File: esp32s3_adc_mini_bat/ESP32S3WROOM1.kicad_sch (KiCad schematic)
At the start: 5 parts, among them J4 Conn_01x22_Socket, J5 Conn_01x22_Socket, U2 ESP32-S3-WROOM-1

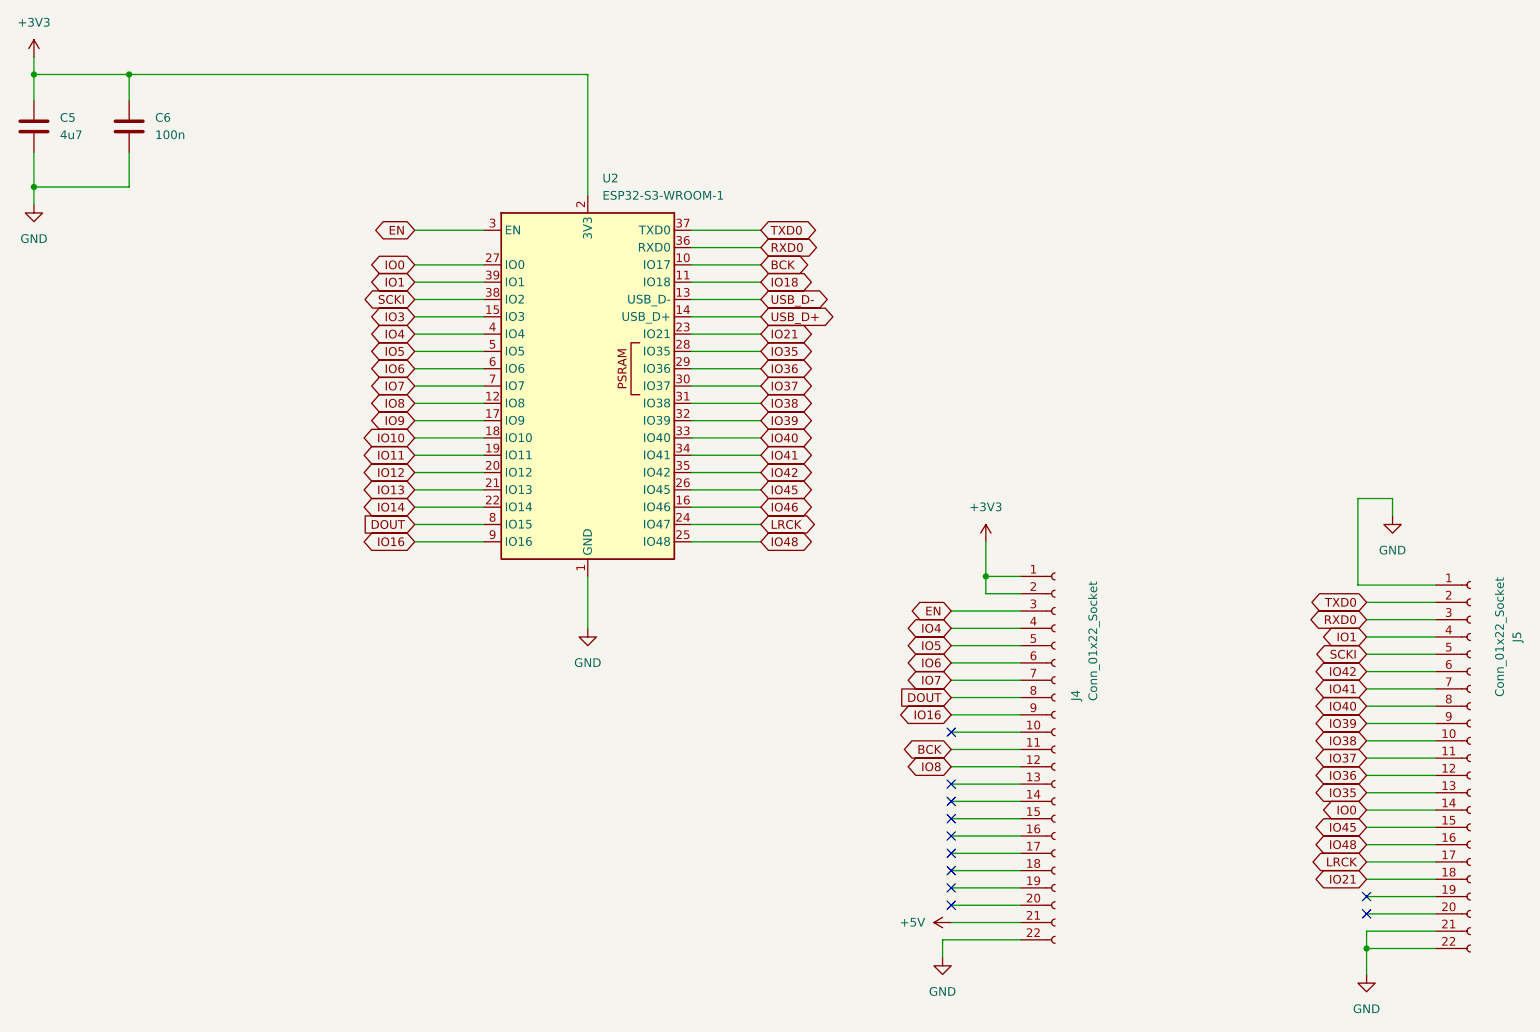
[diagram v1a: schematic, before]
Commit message: feat: schematic done and pcb grouping
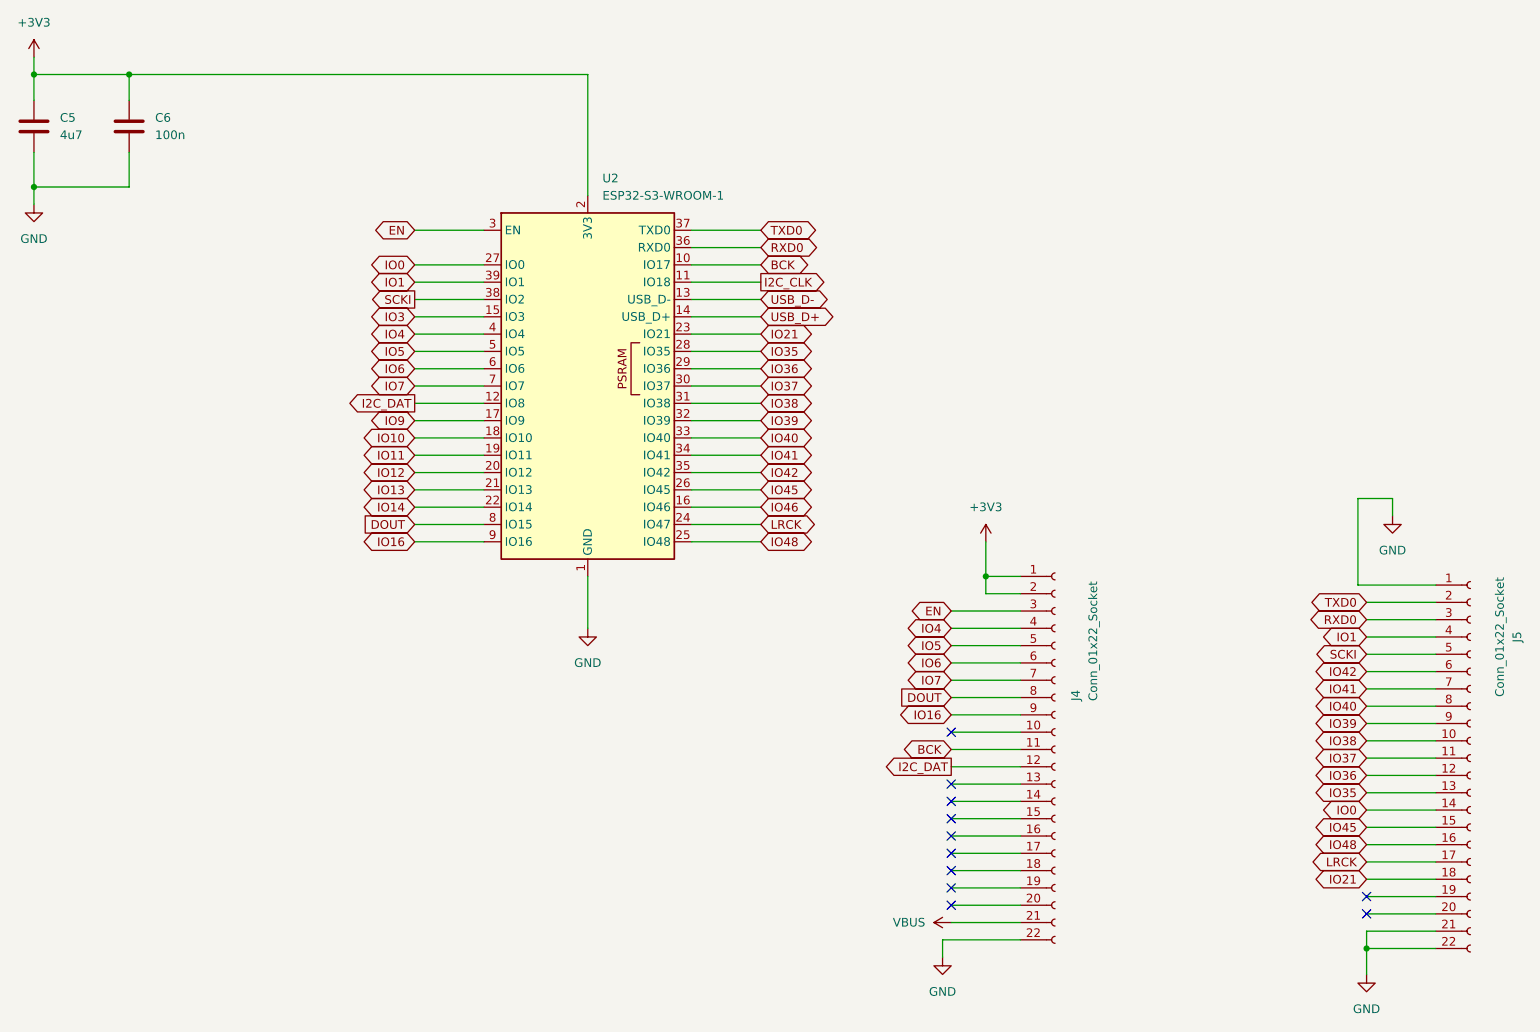
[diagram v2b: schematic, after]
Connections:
- net +5V renamed VBUS
- net IO18 renamed I2C_CLK
- net IO8 renamed I2C_DAT
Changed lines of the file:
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@@
+	(wire
+		(pts
+			(xy 160.02 144.78) (xy 170.18 144.78)
+		)
+		(stroke
+			(width 0)
+			(type default)
+		)
+	)
+	(wire
+		(pts
+			(xy 39.37 41.91) (xy 39.37 36.83)
+		)
+		(stroke
+			(width 0)
+			(type default)
+		)
+	)
+	(wire
+		(pts
+			(xy 25.4 25.4) (xy 25.4 29.21)
+		)
+		(stroke
+			(width 0)
+			(type default)
+		)
+	)
+	(wire
+		(pts
+			(xy 132.08 81.28) (xy 121.92 81.28)
+		)
+		(stroke
+			(width 0)
+			(type default)
+		)
+	)
+	(wire
+		(pts
+			(xy 220.98 133.35) (xy 231.14 133.35)
+		)
+		(stroke
+			(width 0)
+			(type default)
+		)
+	)
+	(wire
+		(pts
+			(xy 160.02 137.16) (xy 170.18 137.16)
+		)
+		(stroke
+			(width 0)
+			(type default)
+		)
+	)
 	(wire
 		(pts
@@
 	(wire
 		(pts
-			(xy 160.02 144.78) (xy 170.18 144.78)
-		)
-		(stroke
-			(width 0)
-			(type default)
-		)
-	)
-	(wire
-		(pts
-			(xy 39.37 41.91) (xy 39.37 36.83)
-		)
-		(stroke
-			(width 0)
-			(type default)
-		)
-	)
-	(wire
-		(pts
-			(xy 25.4 25.4) (xy 25.4 29.21)
-		)
-		(stroke
-			(width 0)
-			(type default)
-		)
-	)
-	(wire
-		(pts
-			(xy 132.08 81.28) (xy 121.92 81.28)
-		)
-		(stroke
-			(width 0)
-			(type default)
-		)
-	)
-	(wire
-		(pts
-			(xy 220.98 133.35) (xy 231.14 133.35)
-		)
-		(stroke
-			(width 0)
-			(type default)
-		)
-	)
-	(wire
-		(pts
-			(xy 160.02 137.16) (xy 170.18 137.16)
-		)
-		(stroke
-			(width 0)
-			(type default)
-		)
-	)
-	(wire
-		(pts
 			(xy 220.98 148.59) (xy 231.14 148.59)
 		)
@@
 	(wire
 		(pts
-			(xy 132.08 55.88) (xy 121.92 55.88)
+			(xy 121.92 55.88) (xy 132.08 55.88)
 		)
 		(stroke
@@
 		)
 	)
-	(global_label "IO8"
-		(shape bidirectional)
-		(at 160.02 127 180)
-		(fields_autoplaced yes)
-		(effects
-			(font
-				(size 1.27 1.27)
-			)
-			(justify right)
-		)
-		(property "Intersheetrefs" "${INTERSHEET_REFS}"
-			(at 152.7787 127 0)
-			(hide yes)
-			(show_name no)
-			(do_not_autoplace no)
-			(effects
-				(font
-					(size 1.27 1.27)
-				)
-				(justify right)
-			)
-		)
-	)
 	(global_label "IO36"
 		(shape bidirectional)
@@
 		)
 	)
-	(global_label "IO18"
-		(shape bidirectional)
+	(global_label "IO42"
+		(shape bidirectional)
+		(at 132.08 83.82 0)
+		(fields_autoplaced yes)
+		(effects
+			(font
+				(size 1.27 1.27)
+			)
+			(justify left)
+		)
+		(property "Intersheetrefs" "${INTERSHEET_REFS}"
+			(at 140.5308 83.82 0)
+			(hide yes)
+			(show_name no)
+			(do_not_autoplace no)
+			(effects
+				(font
+					(size 1.27 1.27)
+				)
+				(justify left)
+			)
+		)
+	)
+	(global_label "IO48"
+		(shape bidirectional)
+		(at 220.98 138.43 180)
+		(fields_autoplaced yes)
+		(effects
+			(font
+				(size 1.27 1.27)
+			)
+			(justify right)
+		)
+		(property "Intersheetrefs" "${INTERSHEET_REFS}"
+			(at 212.5292 138.43 0)
+			(hide yes)
+			(show_name no)
+			(do_not_autoplace no)
+			(effects
+				(font
+					(size 1.27 1.27)
+				)
+				(justify right)
+			)
+		)
+	)
+	(global_label "I2C_CLK"
+		(shape output)
 		(at 132.08 55.88 0)
 		(fields_autoplaced yes)
@@
 		)
 		(property "Intersheetrefs" "${INTERSHEET_REFS}"
-			(at 140.5308 55.88 0)
+			(at 142.6852 55.88 0)
 			(hide yes)
 			(show_name no)
@@
 				)
 				(justify left)
-			)
-		)
-	)
-	(global_label "IO42"
-		(shape bidirectional)
-		(at 132.08 83.82 0)
-		(fields_autoplaced yes)
-		(effects
-			(font
-				(size 1.27 1.27)
-			)
-			(justify left)
-		)
-		(property "Intersheetrefs" "${INTERSHEET_REFS}"
-			(at 140.5308 83.82 0)
-			(hide yes)
-			(show_name no)
-			(do_not_autoplace no)
-			(effects
-				(font
-					(size 1.27 1.27)
-				)
-				(justify left)
-			)
-		)
-	)
-	(global_label "IO48"
-		(shape bidirectional)
-		(at 220.98 138.43 180)
-		(fields_autoplaced yes)
-		(effects
-			(font
-				(size 1.27 1.27)
-			)
-			(justify right)
-		)
-		(property "Intersheetrefs" "${INTERSHEET_REFS}"
-			(at 212.5292 138.43 0)
-			(hide yes)
-			(show_name no)
-			(do_not_autoplace no)
-			(effects
-				(font
-					(size 1.27 1.27)
-				)
-				(justify right)
-			)
-		)
-	)
-	(global_label "IO8"
-		(shape bidirectional)
-		(at 81.28 73.66 180)
-		(fields_autoplaced yes)
-		(effects
-			(font
-				(size 1.27 1.27)
-			)
-			(justify right)
-		)
-		(property "Intersheetrefs" "${INTERSHEET_REFS}"
-			(at 74.0387 73.66 0)
-			(hide yes)
-			(show_name no)
-			(do_not_autoplace no)
-			(effects
-				(font
-					(size 1.27 1.27)
-				)
-				(justify right)
 			)
 		)
@@
 	)
 	(global_label "SCKI"
-		(shape bidirectional)
+		(shape output)
 		(at 81.28 58.42 180)
 		(fields_autoplaced yes)
@@
 		)
 		(property "Intersheetrefs" "${INTERSHEET_REFS}"
-			(at 72.8292 58.42 0)
+			(at 73.9405 58.42 0)
 			(hide yes)
 			(show_name no)
@@
 		)
 	)
+	(global_label "I2C_DAT"
+		(shape output)
+		(at 81.28 73.66 180)
+		(fields_autoplaced yes)
+		(effects
+			(font
+				(size 1.27 1.27)
+			)
+			(justify right)
+		)
+		(property "Intersheetrefs" "${INTERSHEET_REFS}"
+			(at 70.9167 73.66 0)
+			(hide yes)
+			(show_name no)
+			(do_not_autoplace no)
+			(effects
+				(font
+					(size 1.27 1.27)
+				)
+				(justify right)
+			)
+		)
+	)
 	(global_label "IO1"
 		(shape bidirectional)
@@
 				)
 				(justify left)
+			)
+		)
+	)
+	(global_label "I2C_DAT"
+		(shape output)
+		(at 160.02 127 180)
+		(fields_autoplaced yes)
+		(effects
+			(font
+				(size 1.27 1.27)
+			)
+			(justify right)
+		)
+		(property "Intersheetrefs" "${INTERSHEET_REFS}"
+			(at 149.6567 127 0)
+			(hide yes)
+			(show_name no)
+			(do_not_autoplace no)
+			(effects
+				(font
+					(size 1.27 1.27)
+				)
+				(justify right)
 			)
 		)
@@
 			)
 		)
-		(property "Value" "+5V"
+		(property "Value" "VBUS"
 			(at 156.21 149.8599 90)
 			(show_name no)
